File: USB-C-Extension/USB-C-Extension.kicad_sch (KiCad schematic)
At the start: 2 parts, among them J2 USB_C_Receptacle, P2 USB_C_Plug

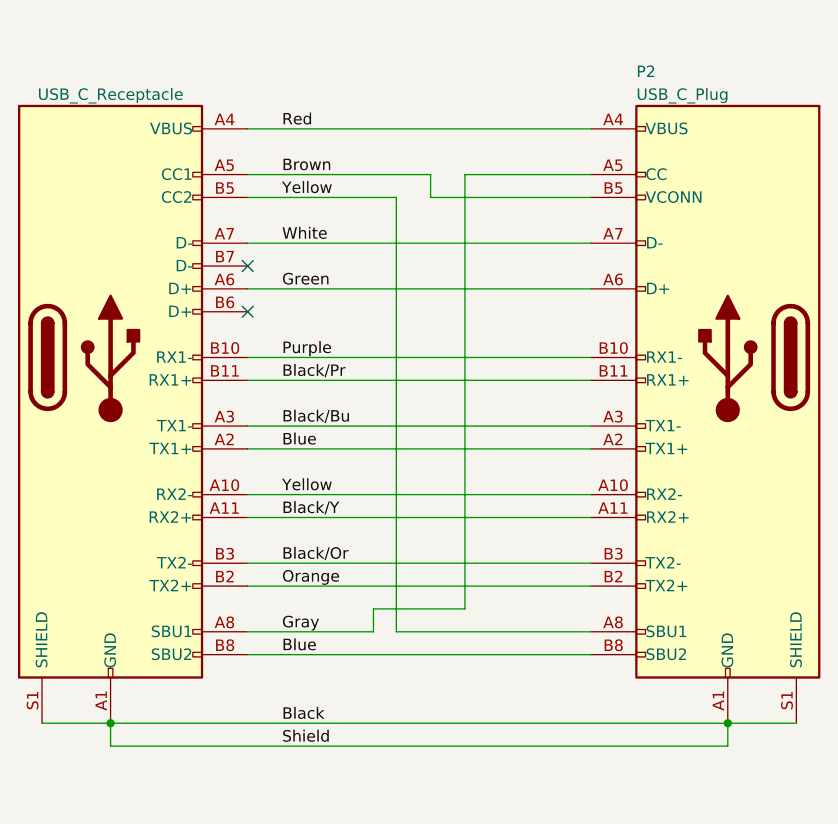
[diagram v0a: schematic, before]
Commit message: add 10 uF power cap
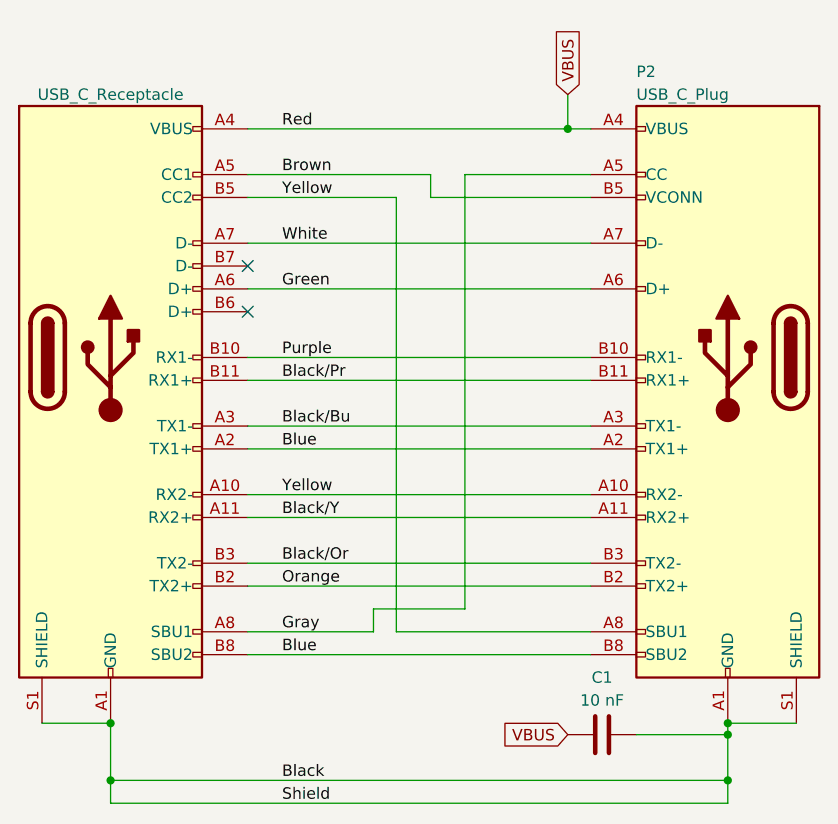
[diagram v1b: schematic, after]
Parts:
- added C1: 10 nF, symbol Device:C
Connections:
- net Black: now also C1.2
- net Red renamed VBUS
- net VBUS: now also C1.1
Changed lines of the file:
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@@
 (kicad_sch (version 20230121) (generator eeschema)
   (paper "A4")
+  (junction (at 85.09 135.89) (diameter 0) (color 0 0 0 0)
+  )
+  (junction (at 153.67 135.89) (diameter 0) (color 0 0 0 0)
+  )
   (junction (at 85.09 129.54) (diameter 0) (color 0 0 0 0)
+  )
+  (junction (at 135.89 63.5) (diameter 0) (color 0 0 0 0)
+  )
+  (junction (at 153.67 130.81) (diameter 0) (color 0 0 0 0)
   )
   (junction (at 153.67 129.54) (diameter 0) (color 0 0 0 0)
@@
     (stroke (width 0) (type default))
   )
+  (wire (pts (xy 85.09 135.89) (xy 85.09 129.54))
+    (stroke (width 0) (type default))
+  )
+  (wire (pts (xy 100.33 63.5) (xy 135.89 63.5))
+    (stroke (width 0) (type default))
+  )
   (wire (pts (xy 120.65 68.58) (xy 120.65 71.12))
     (stroke (width 0) (type default))
@@
     (stroke (width 0) (type default))
   )
-  (wire (pts (xy 85.09 129.54) (xy 153.67 129.54))
+  (wire (pts (xy 153.67 130.81) (xy 153.67 129.54))
+    (stroke (width 0) (type default))
+  )
+  (wire (pts (xy 135.89 63.5) (xy 138.43 63.5))
+    (stroke (width 0) (type default))
+  )
+  (wire (pts (xy 85.09 135.89) (xy 153.67 135.89))
     (stroke (width 0) (type default))
   )
@@
     (stroke (width 0) (type default))
   )
-  (wire (pts (xy 153.67 129.54) (xy 153.67 132.08))
-    (stroke (width 0) (type default))
-  )
   (wire (pts (xy 100.33 106.68) (xy 138.43 106.68))
     (stroke (width 0) (type default))
   )
-  (wire (pts (xy 85.09 132.08) (xy 153.67 132.08))
-    (stroke (width 0) (type default))
-  )
-  (wire (pts (xy 100.33 63.5) (xy 138.43 63.5))
+  (wire (pts (xy 85.09 135.89) (xy 85.09 138.43))
+    (stroke (width 0) (type default))
+  )
+  (wire (pts (xy 135.89 59.69) (xy 135.89 63.5))
+    (stroke (width 0) (type default))
+  )
+  (wire (pts (xy 85.09 138.43) (xy 153.67 138.43))
+    (stroke (width 0) (type default))
+  )
+  (wire (pts (xy 153.67 135.89) (xy 153.67 138.43))
     (stroke (width 0) (type default))
   )
@@
     (stroke (width 0) (type default))
   )
-  (wire (pts (xy 85.09 129.54) (xy 85.09 132.08))
-    (stroke (width 0) (type default))
-  )
   (wire (pts (xy 100.33 91.44) (xy 138.43 91.44))
     (stroke (width 0) (type default))
@@
     (stroke (width 0) (type default))
   )
+  (wire (pts (xy 153.67 130.81) (xy 153.67 135.89))
+    (stroke (width 0) (type default))
+  )
   (wire (pts (xy 124.46 68.58) (xy 124.46 116.84))
     (stroke (width 0) (type default))
@@
     (stroke (width 0) (type default))
   )
+  (wire (pts (xy 143.51 130.81) (xy 153.67 130.81))
+    (stroke (width 0) (type default))
+  )
   (wire (pts (xy 100.33 71.12) (xy 116.84 71.12))
     (stroke (width 0) (type default))
@@
     (effects (font (size 1.27 1.27)) (justify left bottom))
   )
-  (label "Shield" (at 104.14 132.08 0) (fields_autoplaced)
+  (label "Shield" (at 104.14 138.43 0) (fields_autoplaced)
     (effects (font (size 1.27 1.27)) (justify left bottom))
   )
@@
     (effects (font (size 1.27 1.27)) (justify left bottom))
   )
-  (label "Black" (at 104.14 129.54 0) (fields_autoplaced)
-    (effects (font (size 1.27 1.27)) (justify left bottom))
+  (label "Black" (at 104.14 135.89 0) (fields_autoplaced)
+    (effects (font (size 1.27 1.27)) (justify left bottom))
+  )
+  (global_label "VBUS" (shape input) (at 135.89 59.69 90) (fields_autoplaced)
+    (effects (font (size 1.27 1.27)) (justify left))
+    (property "Intersheetrefs" "${INTERSHEET_REFS}" (at 135.89 51.8856 90)
+      (effects (font (size 1.27 1.27)) (justify left) hide)
+    )
+  )
+  (global_label "VBUS" (shape input) (at 135.89 130.81 180) (fields_autoplaced)
+    (effects (font (size 1.27 1.27)) (justify right))
+    (property "Intersheetrefs" "${INTERSHEET_REFS}" (at 128.0856 130.81 0)
+      (effects (font (size 1.27 1.27)) (justify right) hide)
+    )
   )
   (symbol (lib_id "Connector:USB_C_Plug") (at 153.67 88.9 0) (mirror y) (unit 1)
@@
         )
       )
+    )
+  )
+  (symbol (lib_id "Device:C") (at 139.7 130.81 90) (unit 1)
+    (in_bom yes) (on_board yes) (dnp no) (fields_autoplaced)
+    (property "Reference" "C1" (at 139.7 124.46 90)
+      (effects (font (size 1.27 1.27)))
+    )
+    (property "Value" "10 nF" (at 139.7 127 90)
+      (effects (font (size 1.27 1.27)))
+    )
+    (property "Footprint" "" (at 143.51 129.8448 0)
+      (effects (font (size 1.27 1.27)) hide)
+    )
+    (property "Datasheet" "~" (at 139.7 130.81 0)
+      (effects (font (size 1.27 1.27)) hide)
+    )
+    (pin "1")
+    (pin "2")
+    (instances
+      (project "USB-C-Extension"
+        (path "/6dae0cb5-2ff1-4023-9912-8e6d16e6a11e"
+          (reference "C1") (unit 1)
+        )
+      )
